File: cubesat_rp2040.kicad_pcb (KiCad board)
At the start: 4 copper layers, 90.2 x 95.9 mm, 44 parts, among them J1 FTSH-105-01-L-DV-007, J2 Conn_01x02, J3 USB_C_Receptacle_USB2.0, SW1 SW_Push, U1 RP2040, U2 W25Q128JVS, U3 AMS1117-3.3

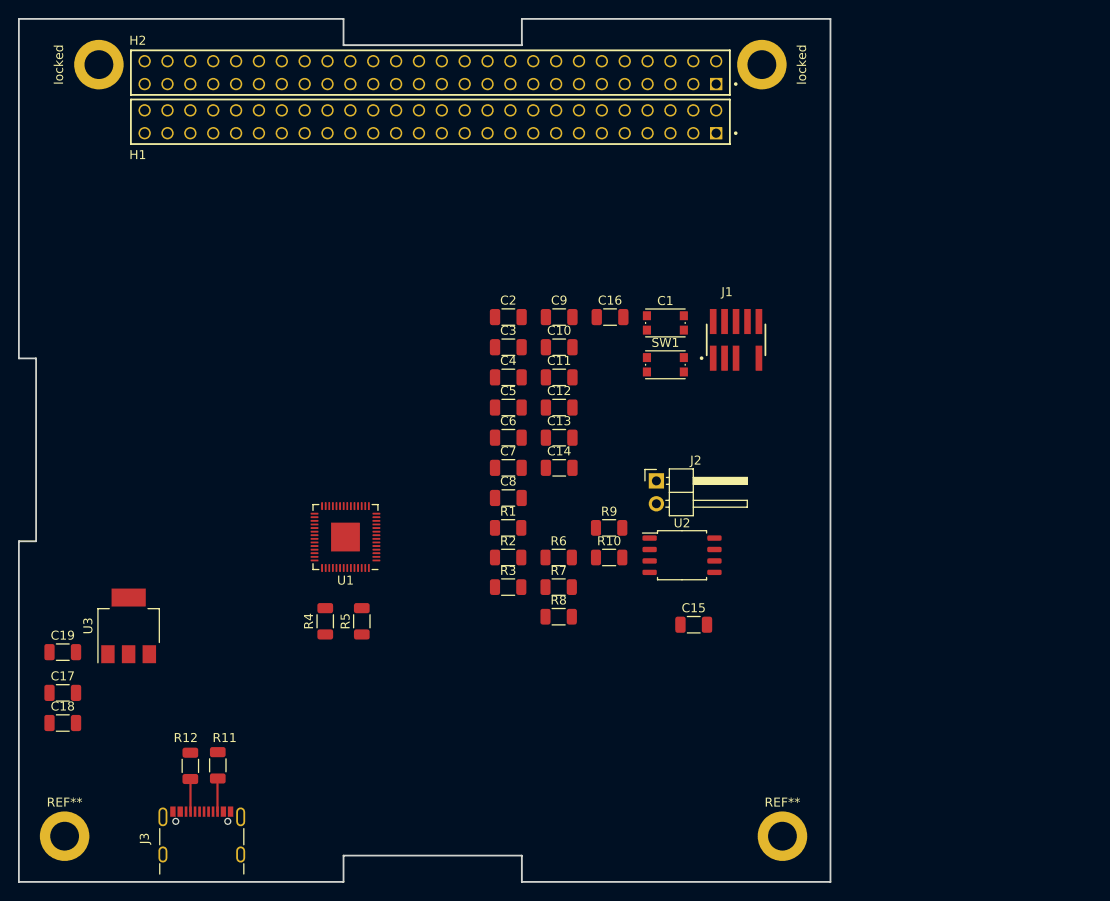
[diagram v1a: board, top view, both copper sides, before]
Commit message: break out subcircuits, add switching regulator
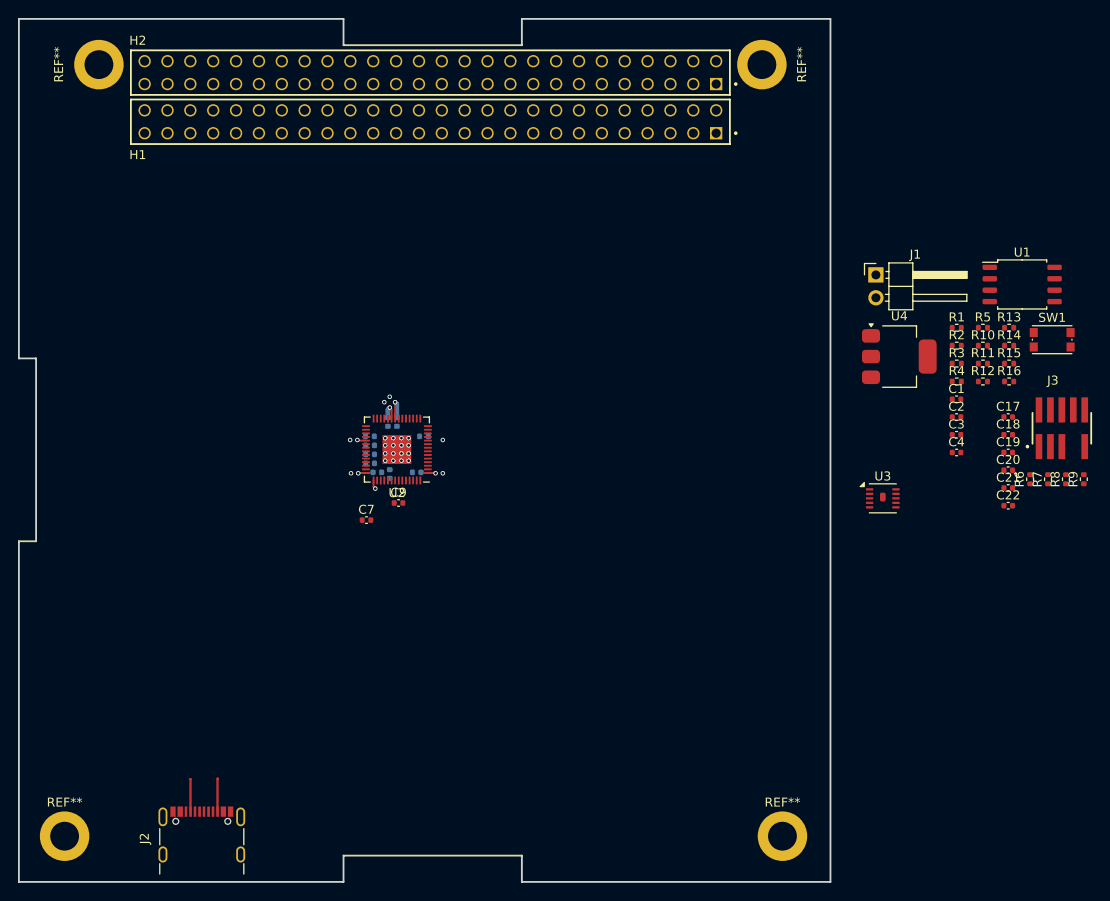
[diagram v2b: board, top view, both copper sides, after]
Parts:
- removed the J1 at (232.1, 92.2)
- removed the R1 at (206.8, 113.1)
- removed the R2 at (206.8, 116.4)
- removed the R3 at (206.8, 119.6)
- added C20: C, Capacitor_SMD:C_0402_1005Metric, F.Cu at (262.3, 106.7)
- added C21: C, Capacitor_SMD:C_0402_1005Metric, F.Cu at (262.3, 108.6)
- added C22: C, Capacitor_SMD:C_0402_1005Metric, F.Cu at (262.3, 110.6)
- added J3: FTSH-105-01-L-DV-007, cubesat_rp2040:SAMTEC_FTSH-105-01-L-DV-007, F.Cu at (268.3, 102.0)
- added R10: 100k, Resistor_SMD:R_0402_1005Metric, F.Cu at (259.5, 92.8)
- added R11: 100k, Resistor_SMD:R_0402_1005Metric, F.Cu at (259.5, 94.8)
- added R12: 100k, Resistor_SMD:R_0402_1005Metric, F.Cu at (259.5, 96.8)
- added R13: R, Resistor_SMD:R_0402_1005Metric, F.Cu at (262.4, 90.8)
- added R14: R, Resistor_SMD:R_0402_1005Metric, F.Cu at (262.4, 92.8)
- added R15: R, Resistor_SMD:R_0402_1005Metric, F.Cu at (262.4, 94.8)
- added R16: R_{FSW}, Resistor_SMD:R_0402_1005Metric, F.Cu at (262.4, 96.8)
- added U4: AMS1117-3.3, Package_TO_SOT_SMD:SOT-223-3_TabPin2, F.Cu at (250.2, 94.0)
- C1: renamed from C13; footprint Capacitor_SMD:C_1206_3216Metric -> Capacitor_SMD:C_0402_1005Metric
- C10: renamed from C4; footprint Capacitor_SMD:C_1206_3216Metric -> Capacitor_SMD:C_0402_1005Metric; moved to B.Cu
- C11: renamed from C5; footprint Capacitor_SMD:C_1206_3216Metric -> Capacitor_SMD:C_0402_1005Metric; moved to B.Cu
- C12: renamed from C6; footprint Capacitor_SMD:C_1206_3216Metric -> Capacitor_SMD:C_0402_1005Metric; moved to B.Cu
- C13: renamed from C7; footprint Capacitor_SMD:C_1206_3216Metric -> Capacitor_SMD:C_0402_1005Metric; moved to B.Cu
- C14: renamed from C8; footprint Capacitor_SMD:C_1206_3216Metric -> Capacitor_SMD:C_0402_1005Metric; moved to B.Cu
- C15: renamed from C9; footprint Capacitor_SMD:C_1206_3216Metric -> Capacitor_SMD:C_0402_1005Metric; moved to B.Cu
- C16: renamed from C10; footprint Capacitor_SMD:C_1206_3216Metric -> Capacitor_SMD:C_0402_1005Metric; moved to B.Cu
- C17, C18, C19: footprint Capacitor_SMD:C_1206_3216Metric -> Capacitor_SMD:C_0402_1005Metric
- C2: renamed from C14; footprint Capacitor_SMD:C_1206_3216Metric -> Capacitor_SMD:C_0402_1005Metric
- C3: renamed from C15; footprint Capacitor_SMD:C_1206_3216Metric -> Capacitor_SMD:C_0402_1005Metric
- C4: renamed from C16; footprint Capacitor_SMD:C_1206_3216Metric -> Capacitor_SMD:C_0402_1005Metric
- C5: renamed from C1; footprint Button_Switch_SMD:SW_Push_1P1T_NO_CK_KMR2 -> Capacitor_SMD:C_0402_1005Metric; moved to B.Cu
- C6: renamed from C2; footprint Capacitor_SMD:C_1206_3216Metric -> Capacitor_SMD:C_0402_1005Metric; moved to B.Cu
- C7: renamed from C11; footprint Capacitor_SMD:C_1206_3216Metric -> Capacitor_SMD:C_0402_1005Metric
- C8: renamed from C3; footprint Capacitor_SMD:C_1206_3216Metric -> Capacitor_SMD:C_0402_1005Metric; moved to B.Cu
- C9: renamed from C12; footprint Capacitor_SMD:C_1206_3216Metric -> Capacitor_SMD:C_0402_1005Metric
- R1: renamed from R9; footprint Resistor_SMD:R_1206_3216Metric -> Resistor_SMD:R_0402_1005Metric
- R2: renamed from R7; footprint Resistor_SMD:R_1206_3216Metric -> Resistor_SMD:R_0402_1005Metric
- R3: renamed from R6; footprint Resistor_SMD:R_1206_3216Metric -> Resistor_SMD:R_0402_1005Metric
- R4: renamed from R10; footprint Resistor_SMD:R_1206_3216Metric -> Resistor_SMD:R_0402_1005Metric
- R5: renamed from R8; footprint Resistor_SMD:R_1206_3216Metric -> Resistor_SMD:R_0402_1005Metric
- R6: renamed from R4; footprint Resistor_SMD:R_1206_3216Metric -> Resistor_SMD:R_0402_1005Metric
- R7: renamed from R5; footprint Resistor_SMD:R_1206_3216Metric -> Resistor_SMD:R_0402_1005Metric
- R8: renamed from R11; footprint Resistor_SMD:R_1206_3216Metric -> Resistor_SMD:R_0402_1005Metric
- R9: renamed from R12; footprint Resistor_SMD:R_1206_3216Metric -> Resistor_SMD:R_0402_1005Metric
- U3: value AMS1117-3.3 -> ~; footprint Package_TO_SOT_SMD:SOT-223-3_TabPin2 -> cubesat_rp2040:DFN-10-1EP_3x3mm_P0.5mm_EP0.98x0.62mm_Offset0.15mm
- moved C18 109.8 mm to (262.3, 102.7)
- moved C17 109.4 mm to (262.3, 100.8)
- moved C19 107.4 mm to (262.3, 104.7)
- moved R9 104.3 mm to (270.7, 107.7)
- moved R8 99.4 mm to (268.7, 107.7)
- moved U3 85.0 mm to (248.4, 109.8), turned to 0 degrees
- moved R6 79.9 mm to (264.8, 107.7)
- moved R7 77.9 mm to (266.7, 107.7)
- moved R5 57.0 mm to (259.5, 90.8)
- moved R2 51.7 mm to (256.6, 92.8)
- moved R3 49.2 mm to (256.6, 94.8)
- moved U1 48.3 mm to (263.9, 86.0)
- moved R1 44.6 mm to (256.6, 90.8)
- moved C2 44.5 mm to (256.6, 100.8)
- moved C1 44.4 mm to (256.6, 98.8)
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- renumbered J2 to J1, J3 to J2, locked to REF**, U2 to U1, U1 to U2
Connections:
- net /USB/USB_D+ renamed /USB.D+
- net /USB/USB_D- renamed /USB.D-
- C17 pad 1: +3V3 -> VBUS
- C19 pad 1: VBUS -> +3V3
- U3 pad 1: +3V3 -> Net-(U3-VOUT/FB)
- U3 pad 2: +3V3 -> unconnected-(U3-VBIAS-Pad2)
- U3 pad 3: VBUS -> Net-(U3-VCC)
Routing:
- net +3V3: track 0.00 -> 7.36 mm, vias 0 -> 5
- net +1V1: track 0.00 -> 2.51 mm, vias 0 -> 1
- net GND: vias 0 -> 22

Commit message: Complete power regulator schematics
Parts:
- removed C1, C2: 33p, Capacitor_SMD:C_0402_1005Metric
- removed C3, C4, C5, C6: 100n, Capacitor_SMD:C_0402_1005Metric
- removed J1: Conn_01x02, Connector_PinHeader_2.54mm:PinHeader_1x02_P2.54mm_Horizontal
- removed J3: FTSH-105-01-L-DV-007, cubesat_rp2040:SAMTEC_FTSH-105-01-L-DV-007
- removed R1, R4: 1k, Resistor_SMD:R_0402_1005Metric
- removed SW1: SW_Push, Button_Switch_SMD:SW_Push_1P1T_NO_CK_KMR2
- removed U2: RP2040, Package_DFN_QFN:QFN-56-1EP_7x7mm_P0.4mm_EP3.2x3.2mm
- removed U4: AMS1117-3.3, Package_TO_SOT_SMD:SOT-223-3_TabPin2
- added C23: 100n, Capacitor_SMD:C_0402_1005Metric, F.Cu at (69.9, 173.0)
- added CIN1: 1u, Capacitor_SMD:C_0402_1005Metric, F.Cu at (72.7, 185.2)
- added COUT1: 1u, Capacitor_SMD:C_0402_1005Metric, F.Cu at (69.9, 175.0)
- added CVCC1: 470n, Capacitor_SMD:C_0402_1005Metric, F.Cu at (72.7, 187.2)
- added J5: Conn_01x02, Resistor_SMD:R_0402_1005Metric, F.Cu at (17.3, 50.8)
- added LSW1: 10u, Resistor_SMD:R_0402_1005Metric, F.Cu at (69.8, 185.2)
- added RD1: 16k, Resistor_SMD:R_0402_1005Metric, F.Cu at (67.1, 175.0)
- added RFSW1: 56k, Resistor_SMD:R_0402_1005Metric, F.Cu at (69.8, 189.2)
- added RU1: 47k, Resistor_SMD:R_0402_1005Metric, F.Cu at (67.1, 177.0)
- C10, C12, C13, C14, C15, C16, C8: moved to F.Cu
- C11: value 100n -> 1u; moved to F.Cu
- C17: value 22u -> 100n
- C18: value 10u -> 100n
- C19: value 22u -> C_Small
- C20, C21, C22: value C -> C_Small
- C7: value 2.2u -> 100n
- C9: value 2.2u -> 1u
- H1, H2: footprint cubesat_rp2040:SAMTEC_ESQ-126-39-G-D -> cubesat_rp2040:ESQ-126-Y-X-D
- J2: value USB_C_Receptacle_USB2.0 -> FTSH-105-01-L-DV-007; footprint Connector_USB:USB_C_Receptacle_GCT_USB4105-xx-A_16P_TopMnt_Horizontal -> cubesat_rp2040:SAMTEC_FTSH-105-01-L-DV-007
- R10, R11, R12: value 100k -> R
- R16: value R_{FSW} -> R
- R2: value 10k -> 100k
- R3: value 400R -> 47k
- R5: value 10k -> R
- R6, R7: value 27R -> R
- R8, R9: value 5.1k -> R
- U1: value W25Q128JVS -> L7983; footprint Package_SO:SOIC-8_5.23x5.23mm_P1.27mm -> cubesat_rp2040:DFN-10-1EP_3x3mm_P0.5mm_EP0.62x0.98mm_Offset0.15mm
- U3: value ~ -> RP2040; footprint cubesat_rp2040:DFN-10-1EP_3x3mm_P0.5mm_EP0.98x0.62mm_Offset0.15mm -> Package_DFN_QFN:QFN-56-1EP_7x7mm_P0.4mm_EP3.2x3.2mm
- moved C17 264.4 mm to (6.67, 33.4)
- moved C18 264.4 mm to (6.67, 35.4)
- moved R9 261.5 mm to (22.9, 24.2), turned to 0 degrees
- moved R8 260.2 mm to (22.9, 22.2), turned to 0 degrees
- moved R7 259.0 mm to (22.9, 20.2), turned to 0 degrees
- moved U3 258.9 mm to (4.16, 23.8)
- moved R10 257.8 mm to (9.56, 29.5)
- moved R11 257.8 mm to (9.56, 31.5)
- moved C20 251.3 mm to (22.2, 32.6)
- moved C21 251.3 mm to (22.2, 34.5)
- moved C22 248.6 mm to (30.7, 20.2)
- moved R14 248.1 mm to (22.3, 30.6)
- moved R6 248.0 mm to (27.9, 34.1), turned to 0 degrees
- moved R15 246.1 mm to (27.9, 20.2)
- moved R16 246.1 mm to (27.9, 22.2)
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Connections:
- C17 pad 1: VBUS -> +3V3
- C20 pad 1: /Power/EXT_VIN -> GND
- C20 pad 2: GND -> /Crystal oscillator/XIN
- C21 pad 1: /Power/PWR_3V3 -> GND
- C21 pad 2: GND -> Net-(C21-Pad2)
- C22 pad 1: Net-(U3-VCC) -> /Debug/RUN
- C8 pad 1: +3V3 -> +1V1
- C9 pad 1: +3V3 -> +1V1
- R10 pad 1: /SWDIO -> /RP2040/USB.D+
- R10 pad 2: +3V3 -> Net-(U3-USB_DP)
- R11 pad 1: GND -> /RP2040/USB.D-
- R11 pad 2: /SWDCLK -> Net-(U3-USB_DM)
- R12 pad 1: /RUN -> /Flash/QSPI.~{SS}
- R12 pad 2: +3V3 -> /Flash/~{USB_BOOT}
- R13 pad 1: unconnected-(R13-Pad1) -> +3V3
- R13 pad 2: /Power/PWR_RST -> /Flash/QSPI.~{SS}
- R14 pad 1: /Power/PWR_3V3 -> Net-(C21-Pad2)
- R14 pad 2: Net-(U3-VOUT/FB) -> /Crystal oscillator/XOUT
- R15 pad 1: Net-(U3-VOUT/FB) -> /Debug/RUN
- R15 pad 2: GND -> Net-(R15-Pad2)
- R16 pad 1: Net-(U3-VCC) -> +3V3
- R16 pad 2: Net-(U3-FSW) -> /Debug/RUN
- R2 pad 1: +3V3 -> /VBUS
- R2 pad 2: /QSPI_SS -> /Debug/RUN
- R3 pad 1: Net-(C2-Pad2) -> /LNM_ENABLE
- R3 pad 2: /XOUT -> GND
- R5 pad 1: +3V3 -> /USB Type-C connector/USB_CC2
- R5 pad 2: /RUN -> GND
- R6 pad 1: /USB.D+ -> /USB Type-C connector/USB_CC1
- R6 pad 2: Net-(U2-USB_DP) -> GND
- R7 pad 1: /USB.D- -> /Debug/SWDIO
- R7 pad 2: Net-(U2-USB_DM) -> +3V3
- R8 pad 1: /USB/USB_CC2 -> GND
- R8 pad 2: GND -> /Debug/SWDCLK
- R9 pad 1: /USB/USB_CC1 -> /Debug/RUN
- R9 pad 2: GND -> +3V3
- U1 pad 1: /QSPI_SS -> Net-(U1-VOUT/FB)
- U1 pad 2: /QSPI_SD1 -> +3V3
- U1 pad 3: /QSPI_SD2 -> /Power/VCC
- U1 pad 4: GND -> /Power/FSW
- U1 pad 5: /QSPI_SD0 -> /LNM_ENABLE
- U1 pad 6: /QSPI_SCLK -> /Debug/RUN
- U1 pad 7: /QSPI_SD3 -> /VBUS
- U1 pad 8: +3V3 -> /VBUS
- U3 pad 1: Net-(U3-VOUT/FB) -> +3V3
- U3 pad 10: GND -> +3V3
- U3 pad 11: (no net) -> unconnected-(U3-GPIO8-Pad11)
- U3 pad 2: unconnected-(U3-VBIAS-Pad2) -> /LNM_ENABLE
- U3 pad 3: Net-(U3-VCC) -> unconnected-(U3-GPIO1-Pad3)
- U3 pad 4: Net-(U3-FSW) -> unconnected-(U3-GPIO2-Pad4)
- U3 pad 5: GND -> unconnected-(U3-GPIO3-Pad5)
- U3 pad 6: /Power/PWR_RST -> unconnected-(U3-GPIO4-Pad6)
- U3 pad 7: /Power/EXT_VIN -> unconnected-(U3-GPIO5-Pad7)
- U3 pad 8: /Power/EXT_VIN -> unconnected-(U3-GPIO6-Pad8)
- U3 pad 9: Net-(U3-LX) -> unconnected-(U3-GPIO7-Pad9)
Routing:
- net +3V3: track 7.36 -> 0.00 mm, vias 5 -> 0
- net /USB/USB_CC2: track 3.70 -> 0.00 mm
- net /USB/USB_CC1: track 3.64 -> 0.00 mm
- net +1V1: track 2.51 -> 0.00 mm, vias 1 -> 0
- net GND: vias 22 -> 0
- removed copper zone on In1.Cu, net GND
- removed copper zone on In2.Cu, net GND

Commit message: Update footprints, route switching regulator circuit block
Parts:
- added J1: USB_C_Receptacle_USB2.0, Connector_USB:USB_C_Receptacle_Amphenol_12401548E4-2A, F.Cu at (174.8, 144.0)
- added SW1: SW_Push, Button_Switch_SMD:SW_Push_1P1T_NO_6x6mm_H9.5mm, F.Cu at (89.3, 132.1)
- added U4: W25Q128JVS, Package_SO:SOIC-8_5.23x5.23mm_P1.27mm, F.Cu at (225.0, 82.0)
- C10, C11, C12, C13, C14, C15, C16, C17, C18, C7, C8, C9: moved to B.Cu
- CIN1, COUT1: footprint Capacitor_SMD:C_0402_1005Metric -> Capacitor_SMD:C_0805_2012Metric
- LSW1: footprint Resistor_SMD:R_0402_1005Metric -> Inductor_SMD:L_1210_3225Metric
- moved C7 234.3 mm to (226.0, 94.5), turned to 90 degrees
- moved R7 234.1 mm to (224.1, 140.0)
- moved R8 234.1 mm to (224.1, 142.0)
- moved R9 234.1 mm to (224.1, 144.0)
- moved J2 234.1 mm to (218.7, 143.2)
- moved R10 232.4 mm to (231.3, 99.0)
- moved R11 232.4 mm to (231.3, 101.0)
- moved C8 231.6 mm to (224.9, 90.5), turned to -90 degrees
- moved C12 231.0 mm to (226.4, 93.0), turned to 180 degrees
- moved U3 230.7 mm to (224.4, 92.4)
- moved C13 230.2 mm to (226.4, 92.0), turned to 180 degrees
- moved C14 229.5 mm to (226.4, 91.0), turned to 180 degrees
- moved C10 228.6 mm to (222.4, 92.0)
- moved C9 228.2 mm to (221.9, 90.5), turned to -90 degrees
- moved C15 227.9 mm to (226.4, 90.0), turned to 180 degrees
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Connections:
- U1 pad 11: (no net) -> GND
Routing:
- net +3V3: track 0.00 -> 33.6 mm, vias 0 -> 6
- net /Flash/QSPI.SD3: track 0.00 -> 14.5 mm
- net /Flash/QSPI.SCLK: track 0.00 -> 13.0 mm
- net +1V1: track 0.00 -> 11.2 mm, vias 0 -> 3
- net /Flash/QSPI.~{SS}: track 0.00 -> 11.0 mm
- net /Flash/QSPI.SD0: track 0.00 -> 9.74 mm
- net /Flash/QSPI.SD1: track 0.00 -> 9.64 mm
- net /Flash/QSPI.SD2: track 0.00 -> 8.29 mm
- net /VBUS: track 0.00 -> 5.10 mm
- net Net-(U1-LX): track 0.00 -> 4.60 mm
- net Net-(U1-VOUT/FB): track 0.00 -> 2.39 mm
- net /Power/FSW: track 0.00 -> 1.78 mm
- net /LNM_ENABLE: track 0.00 -> 1.72 mm
- net /Power/VCC: track 0.00 -> 1.49 mm
- net /Debug/RUN: track 0.00 -> 1.46 mm
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- added copper zone on F.Cu, net +3V3
- added copper zone on B.Cu, net GND
- added copper zone on F.Cu, net GND
- added copper zone on In1.Cu, net GND
- added copper zone on In2.Cu, net GND
